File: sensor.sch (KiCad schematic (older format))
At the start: 1 part, among them J1 connector

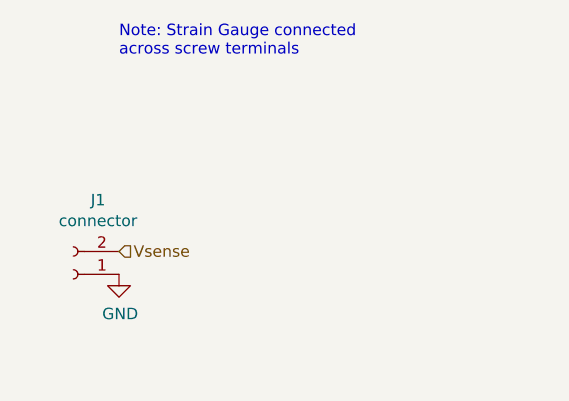
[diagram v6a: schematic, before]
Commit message: updated sch with pico connectors
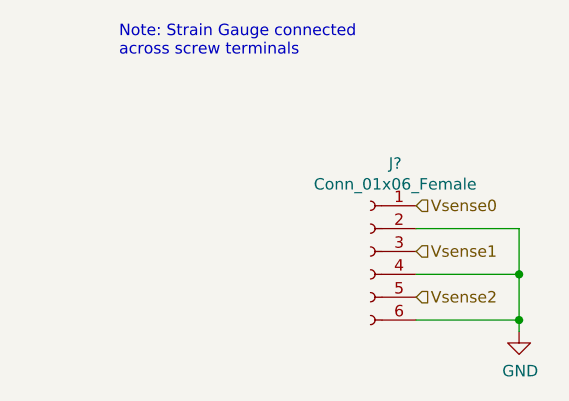
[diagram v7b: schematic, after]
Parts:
- removed J1: connector, Connector_PinHeader_1.27mm:PinHeader_1x02_P1.27mm_Vertical, symbol Connector:Conn_01x02_Female
- added J?: Conn_01x06_Female, Connector_Molex:Molex_Pico-Clasp_202396-0607_1x06-1MP_P1.00mm_Horizontal, symbol Connector:Conn_01x06_Female
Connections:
- net GND: now also J?.2 (Pin_2), J?.4 (Pin_4), J?.6 (Pin_6)
- new net Vsense0: J?.1 (Pin_1)
- new net Vsense1: J?.3 (Pin_3)
- new net Vsense2: J?.5 (Pin_5)
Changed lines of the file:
@@
 $Descr A4 11693 8268
 encoding utf-8
-Sheet 3 41
+Sheet 4 21
 Title ""
 Date ""
@@
 Comment4 ""
 $EndDescr
-Text HLabel 3900 3900 2    50   Input ~ 0
-Vsense
+Text HLabel 5200 3700 2    50   Input ~ 0
+Vsense0
 Text Notes 3900 3050 0    50   ~ 0
 Note: Strain Gauge connected\nacross screw terminals
@@
 L power:GND #PWR?
 U 1 1 60194B46
-P 3900 4000
+P 5650 4250
 AR Path="/60132BC3/6013AE22/60194B46" Ref="#PWR?"  Part="1"
 AR Path="/6017CC5E/60194B46" Ref="#PWR?"  Part="1"
@@
 AR Path="/601B4C19/601A6FD1/60194B46" Ref="#PWR074"  Part="1"
 AR Path="/601B4C19/601A6FD6/60194B46" Ref="#PWR075"  Part="1"
-F 0 "#PWR016" H 3900 3750 50  0001 C CNN
-F 1 "GND" H 3905 3827 50  0000 C CNN
-F 2 "" H 3900 4000 50  0001 C CNN
-F 3 "" H 3900 4000 50  0001 C CNN
-	1    3900 4000
+F 0 "#PWR017" H 5650 4000 50  0001 C CNN
+F 1 "GND" H 5655 4077 50  0000 C CNN
+F 2 "" H 5650 4250 50  0001 C CNN
+F 3 "" H 5650 4250 50  0001 C CNN
+	1    5650 4250
 	1    0    0    -1
 $EndComp
 $Comp
-L Connector:Conn_01x02_Female J1
-U 1 1 60B3291B
-P 3700 4000
-AR Path="/6017CC5E/60194350/60B3291B" Ref="J1"  Part="1"
-AR Path="/6017CC5E/6019B999/60B3291B" Ref="J2"  Part="1"
-AR Path="/6017CC5E/6019BDB6/60B3291B" Ref="J3"  Part="1"
-AR Path="/601927EB/601A1EA6/60B3291B" Ref="J4"  Part="1"
-AR Path="/601927EB/601A1EAB/60B3291B" Ref="J5"  Part="1"
-AR Path="/601927EB/601A1EB0/60B3291B" Ref="J6"  Part="1"
-AR Path="/6019C043/601A47AA/60B3291B" Ref="J7"  Part="1"
-AR Path="/6019C043/601A47AF/60B3291B" Ref="J8"  Part="1"
-AR Path="/6019C043/601A47B4/60B3291B" Ref="J9"  Part="1"
-AR Path="/6019DBCE/601A6FCC/60B3291B" Ref="J10"  Part="1"
-AR Path="/6019DBCE/601A6FD1/60B3291B" Ref="J11"  Part="1"
-AR Path="/6019DBCE/601A6FD6/60B3291B" Ref="J12"  Part="1"
-AR Path="/601B4C0E/60194350/60B3291B" Ref="J13"  Part="1"
-AR Path="/601B4C0E/6019B999/60B3291B" Ref="J14"  Part="1"
-AR Path="/601B4C0E/6019BDB6/60B3291B" Ref="J15"  Part="1"
-AR Path="/601B4C11/601A1EA6/60B3291B" Ref="J16"  Part="1"
-AR Path="/601B4C11/601A1EAB/60B3291B" Ref="J17"  Part="1"
-AR Path="/601B4C11/601A1EB0/60B3291B" Ref="J18"  Part="1"
-AR Path="/601B4C16/601A47AA/60B3291B" Ref="J19"  Part="1"
-AR Path="/601B4C16/601A47AF/60B3291B" Ref="J20"  Part="1"
-AR Path="/601B4C16/601A47B4/60B3291B" Ref="J21"  Part="1"
-AR Path="/601B4C19/601A6FCC/60B3291B" Ref="J22"  Part="1"
-AR Path="/601B4C19/601A6FD1/60B3291B" Ref="J23"  Part="1"
-AR Path="/601B4C19/601A6FD6/60B3291B" Ref="J24"  Part="1"
-AR Path="/601B73B7/60194350/60B3291B" Ref="J25"  Part="1"
-AR Path="/601B73B7/6019B999/60B3291B" Ref="J26"  Part="1"
-AR Path="/601B73B7/6019BDB6/60B3291B" Ref="J27"  Part="1"
-AR Path="/601B73BA/601A1EA6/60B3291B" Ref="J28"  Part="1"
-AR Path="/601B73BA/601A1EAB/60B3291B" Ref="J29"  Part="1"
-AR Path="/601B73BA/601A1EB0/60B3291B" Ref="J30"  Part="1"
-F 0 "J1" H 3592 3675 50  0000 C CNN
-F 1 "connector" H 3592 3766 50  0000 C CNN
-F 2 "Connector_PinHeader_1.27mm:PinHeader_1x02_P1.27mm_Vertical" H 3700 4000 50  0001 C CNN
-F 3 "~" H 3700 4000 50  0001 C CNN
-	1    3700 4000
-	-1   0    0    1
+L Connector:Conn_01x06_Female J?
+U 1 1 60B45C6C
+P 5000 3900
+F 0 "J?" H 4892 4285 50  0000 C CNN
+F 1 "Conn_01x06_Female" H 4892 4194 50  0000 C CNN
+F 2 "Connector_Molex:Molex_Pico-Clasp_202396-0607_1x06-1MP_P1.00mm_Horizontal" H 5000 3900 50  0001 C CNN
+F 3 "https://www.digikey.com/en/products/detail/molex/5013300600/1531503?s=N4IgjCBcoLQBxVAYygMwIYBsDOBTANCAPZQDaIAnAAxUgC6Avg4QExkgCsVYAzDzQDYa9BkA" H 5000 3900 50  0001 C CNN
+	1    5000 3900
+	-1   0    0    -1
 $EndComp
+Wire Wire Line
+	5200 3800 5650 3800
+Wire Wire Line
+	5650 3800 5650 4000
+Connection ~ 5650 4000
+Wire Wire Line
+	5650 4000 5650 4200
+Wire Wire Line
+	5200 4000 5650 4000
+Connection ~ 5650 4200
+Wire Wire Line
+	5650 4200 5650 4250
+Wire Wire Line
+	5200 4200 5650 4200
+Text HLabel 5200 3900 2    50   Input ~ 0
+Vsense1
+Text HLabel 5200 4100 2    50   Input ~ 0
+Vsense2
 $EndSCHEMATC

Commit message: left off reworking bottom of board
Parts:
- J1: renamed from J?; footprint Connector_Molex:Molex_Pico-Clasp_202396-0607_1x06-1MP_P1.00mm_Horizontal -> Connector_Molex:Molex_PicoBlade_53047-0610_1x06_P1.25mm_Vertical
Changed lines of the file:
@@
 $Descr A4 11693 8268
 encoding utf-8
-Sheet 4 21
+Sheet 3 21
 Title ""
 Date ""
@@
 AR Path="/601B4C19/601A6FD1/60194B46" Ref="#PWR074"  Part="1"
 AR Path="/601B4C19/601A6FD6/60194B46" Ref="#PWR075"  Part="1"
-F 0 "#PWR017" H 5650 4000 50  0001 C CNN
+F 0 "#PWR016" H 5650 4000 50  0001 C CNN
 F 1 "GND" H 5655 4077 50  0000 C CNN
 F 2 "" H 5650 4250 50  0001 C CNN
@@
 U 1 1 60B45C6C
 P 5000 3900
-F 0 "J?" H 4892 4285 50  0000 C CNN
+AR Path="/6017CC5E/6019B999/60B45C6C" Ref="J?"  Part="1"
+AR Path="/6017CC5E/60194350/60B45C6C" Ref="J1"  Part="1"
+AR Path="/601927EB/601A1EA6/60B45C6C" Ref="J2"  Part="1"
+AR Path="/6019C043/601A47AA/60B45C6C" Ref="J3"  Part="1"
+AR Path="/6019DBCE/601A6FCC/60B45C6C" Ref="J4"  Part="1"
+AR Path="/601B4C0E/60194350/60B45C6C" Ref="J5"  Part="1"
+AR Path="/601B4C11/601A1EA6/60B45C6C" Ref="J6"  Part="1"
+AR Path="/601B4C16/601A47AA/60B45C6C" Ref="J7"  Part="1"
+AR Path="/601B4C19/601A6FCC/60B45C6C" Ref="J8"  Part="1"
+AR Path="/601B73B7/60194350/60B45C6C" Ref="J9"  Part="1"
+AR Path="/601B73BA/601A1EA6/60B45C6C" Ref="J10"  Part="1"
+F 0 "J1" H 4892 4285 50  0000 C CNN
 F 1 "Conn_01x06_Female" H 4892 4194 50  0000 C CNN
-F 2 "Connector_Molex:Molex_Pico-Clasp_202396-0607_1x06-1MP_P1.00mm_Horizontal" H 5000 3900 50  0001 C CNN
+F 2 "Connector_Molex:Molex_PicoBlade_53047-0610_1x06_P1.25mm_Vertical" H 5000 3900 50  0001 C CNN
 F 3 "https://www.digikey.com/en/products/detail/molex/5013300600/1531503?s=N4IgjCBcoLQBxVAYygMwIYBsDOBTANCAPZQDaIAnAAxUgC6Avg4QExkgCsVYAzDzQDYa9BkA" H 5000 3900 50  0001 C CNN
 	1    5000 3900
